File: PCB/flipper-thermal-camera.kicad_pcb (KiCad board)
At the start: 2 copper layers, 1 part, among them U1 MLX90640ESF-BAB-000-SP

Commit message: finish schematic
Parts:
- added C1: 100nF, Capacitor_SMD:C_0805_2012Metric, F.Cu at (81.9, 40.0)
- added C2: 100nF, Capacitor_SMD:C_0805_2012Metric, F.Cu at (81.9, 43.0)
- added C3: 100nF, Capacitor_SMD:C_0805_2012Metric, F.Cu at (81.9, 46.0)
- added C4: 100nF, Capacitor_SMD:C_0805_2012Metric, F.Cu at (81.9, 49.0)
- added C5: 1uF, Capacitor_SMD:C_0805_2012Metric, F.Cu at (81.9, 52.0)
- added C6: 4.7uF, Capacitor_SMD:C_0805_2012Metric, F.Cu at (81.9, 55.1)
- added D1: LED_R, LED_SMD:LED_0805_2012Metric, F.Cu at (86.4, 60.2)
- added D2: LED_G, LED_SMD:LED_0805_2012Metric, F.Cu at (86.4, 63.2)
- added IC1: VEML7700-TT, Components:XDCR_VEML7700-TT, F.Cu at (87.5, 54.5)
- added J1: Conn_01x08, Connector_PinHeader_2.54mm:PinHeader_1x08_P2.54mm_Horizontal, F.Cu at (148.5, 93.0)
- added J2: Conn_01x10, Connector_PinHeader_2.54mm:PinHeader_1x10_P2.54mm_Horizontal, F.Cu at (181.5, 93.0)
- added R1: 2.2k, Resistor_SMD:R_0805_2012Metric, F.Cu at (86.3, 40.0)
- added R2: 2.2k, Resistor_SMD:R_0805_2012Metric, F.Cu at (86.3, 42.9)
- added R3: 1.5k, Resistor_SMD:R_0805_2012Metric, F.Cu at (86.3, 45.9)
- added R4: 10k, Resistor_SMD:R_0805_2012Metric, F.Cu at (86.3, 48.8)
- added U2: XC6206PxxxMR, Package_TO_SOT_SMD:SOT-23-3, F.Cu at (91.1, 40.7)
- added U3: ICM-20948, Sensor_Motion:InvenSense_QFN-24_3x3mm_P0.4mm, F.Cu at (91.1, 45.5)
- added U4: SHT31-DIS, Sensor_Humidity:Sensirion_DFN-8-1EP_2.5x2.5mm_P0.5mm_EP1.1x1.7mm, F.Cu at (138.2, 70.5)
- moved U1 44.1 mm to (154.5, 68.9)
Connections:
- U1 pad 1: unconnected-(U1-SDA-Pad1) -> /SDA
- U1 pad 2: unconnected-(U1-VDD-Pad2) -> +3V3
- U1 pad 3: unconnected-(U1-GND-Pad3) -> GND
- U1 pad 4: unconnected-(U1-SCL-Pad4) -> /SCL
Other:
- board text added: "1"
- board text added: "10"
- board text added: "11"
- board text added: "12"
- board text added: "13"
- board text added: "14"
- board text added: "15"
- board text added: "16"
- board text added: "17"
- board text added: "18"
- board text added: "2"
- board text added: "3"
- board text added: "4"
- board text added: "5"
- board text added: "6"
- board text added: "7"
- board text added: "8"
- board text added: "9"

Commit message: finish routing pcb
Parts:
- removed J1: Conn_01x08, Connector_PinHeader_2.54mm:PinHeader_1x08_P2.54mm_Horizontal
- removed J2: Conn_01x10, Connector_PinHeader_2.54mm:PinHeader_1x10_P2.54mm_Horizontal
- added A1: Flipper_Zero, Module:Flipper_Zero_Angled, F.Cu at (123.5, 88.2)
- IC1, U1: moved to B.Cu
- moved C1 105.3 mm to (181.8, 73.4)
- moved R2 100.1 mm to (178.4, 82.2), turned to 90 degrees
- moved R1 99.5 mm to (176.4, 82.2), turned to 90 degrees
- moved C3 97.5 mm to (176.5, 69.8), turned to 90 degrees
- moved C2 95.8 mm to (171.8, 76.2), turned to 90 degrees
- moved U3 90.9 mm to (176.7, 76.2), turned to 180 degrees
- moved R4 82.8 mm to (164.6, 76.0), turned to 90 degrees
- moved C4 78.4 mm to (151.8, 84.6), turned to 180 degrees
- moved IC1 67.3 mm to (153.2, 69.4), turned to 90 degrees
- moved C5 57.3 mm to (130.6, 82.3), turned to -90 degrees
- moved U2 54.7 mm to (126.9, 82.1), turned to -90 degrees
- moved C6 50.6 mm to (127.1, 77.9), turned to 180 degrees
- moved R3 48.1 mm to (120.8, 79.5), turned to -90 degrees
- moved D2 40.1 mm to (126.0, 69.5)
- moved D1 37.1 mm to (122.2, 69.5)
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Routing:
- net +3V3: track 0.00 -> 154.9 mm, vias 0 -> 2
- net /SDA: track 0.00 -> 62.9 mm, vias 0 -> 1
- net /SCL: track 0.00 -> 53.9 mm, vias 0 -> 3
- net +5V: track 0.00 -> 19.0 mm
- net GND: track 0.00 -> 16.5 mm, vias 0 -> 44
- net /INT_1: track 0.00 -> 16.4 mm, vias 0 -> 1
- net /TMP_RST: track 0.00 -> 14.1 mm, vias 0 -> 1
- net Net-(D1-A): track 0.00 -> 10.1 mm
- net Net-(U3-REGOUT): track 0.00 -> 4.07 mm
- added copper zone on B.Cu, net GND
- added copper zone on F.Cu, net GND
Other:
- board outline added: 67.4 x 20 mm
- board text added: "3V3"
- board text added: "5V"
- board text added: "Flipper Thermal Camera By Evan Yu"
- board text added: "v1.0"

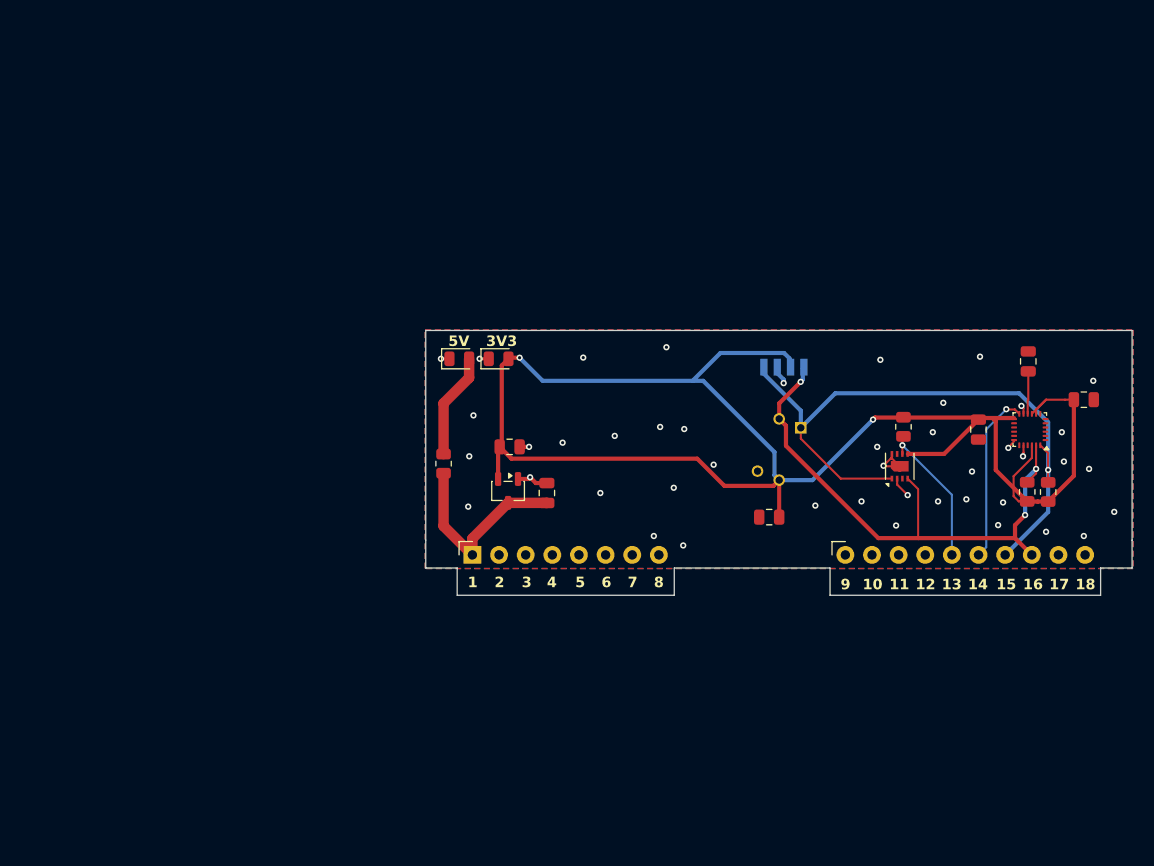
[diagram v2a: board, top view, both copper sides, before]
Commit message: add testpoints
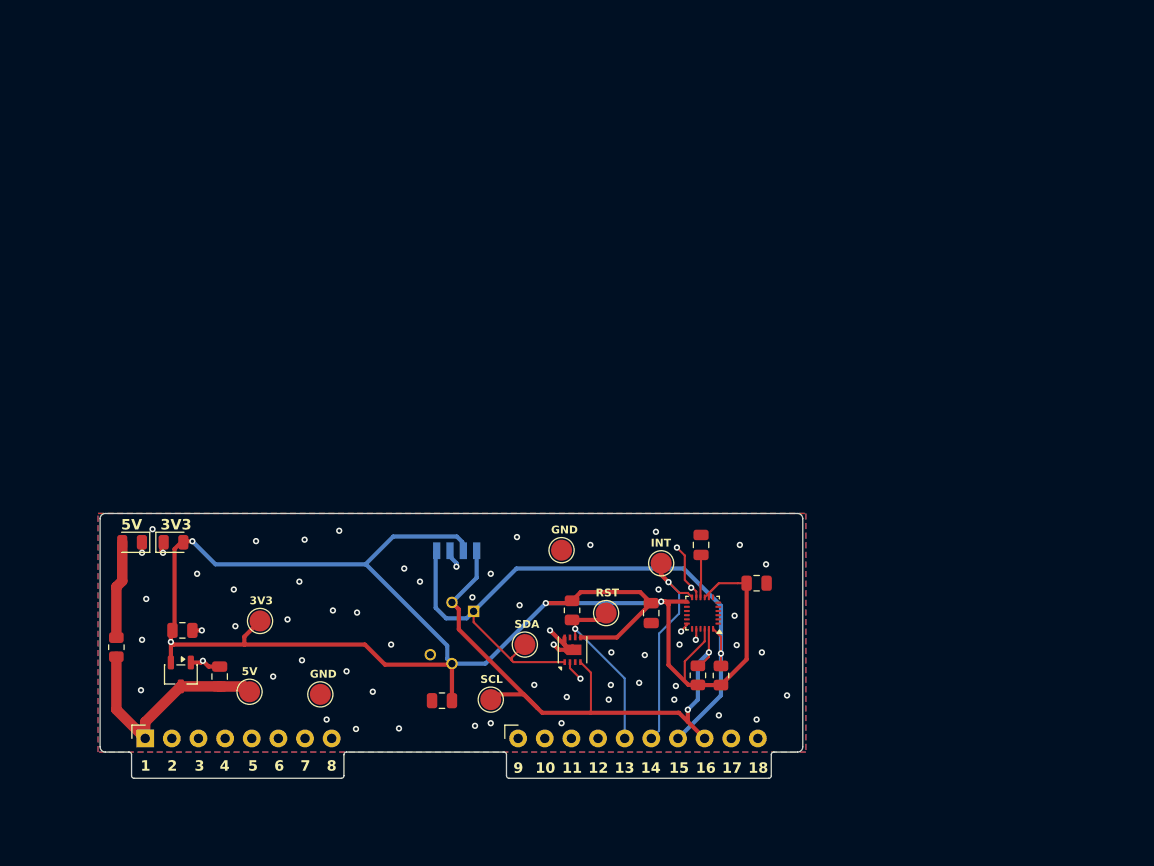
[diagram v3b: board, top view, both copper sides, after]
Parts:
- added SDA1: GND, TestPoint:TestPoint_Pad_D2.0mm, F.Cu at (128.5, 96.8)
- added TP1: 3V3, TestPoint:TestPoint_Pad_D2.0mm, F.Cu at (103.2, 94.5)
- added TP2: 5V, TestPoint:TestPoint_Pad_D2.0mm, F.Cu at (102.2, 101.2)
- added TP3: GND, TestPoint:TestPoint_Pad_D2.0mm, F.Cu at (109.0, 101.5)
- added TP4: GND, TestPoint:TestPoint_Pad_D2.0mm, F.Cu at (132.0, 87.8)
- added TP5: SCL, TestPoint:TestPoint_Pad_D2.0mm, F.Cu at (125.2, 102.0)
- added TP6: TMP_SENS_RST, TestPoint:TestPoint_Pad_D2.0mm, F.Cu at (136.2, 93.8)
- added TP7: INT_ICM, TestPoint:TestPoint_Pad_D2.0mm, F.Cu at (141.5, 89.0)
- moved R4 36.1 mm to (133.0, 93.5)
- moved R1 35.9 mm to (145.0, 99.7)
- moved C1 35.8 mm to (150.6, 90.9)
- moved C4 35.8 mm to (120.6, 102.1)
- moved R2 35.8 mm to (147.2, 99.7)
- moved U3 35.8 mm to (145.4, 93.8)
- moved A1 35.8 mm to (92.3, 105.7)
- moved D1 35.8 mm to (91.0, 87.0), turned to 180 degrees
- moved R3 35.8 mm to (89.5, 97.0)
- moved U1 35.8 mm to (121.5, 95.7)
- moved U2 35.8 mm to (95.7, 99.6)
- moved C2 35.8 mm to (140.6, 93.8)
- moved C3 35.8 mm to (145.3, 87.2)
- moved C5 35.8 mm to (99.4, 99.8)
- moved C6 35.8 mm to (95.9, 95.4)
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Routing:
- net +3V3: track 154.9 -> 168.1 mm, vias 2 -> 4
- net GND: track 16.5 -> 23.0 mm, vias 44 -> 64
- net /SDA: track 62.9 -> 67.9 mm
- net /INT_1: track 16.4 -> 21.4 mm
- net /SCL: track 53.9 -> 57.8 mm, vias 3 -> 2
- net /TMP_RST: track 14.1 -> 17.5 mm
- net +5V: track 19.0 -> 22.1 mm
- net Net-(D1-A): track 10.1 -> 9.32 mm
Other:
- board size 67.4 x 20 mm -> 67 x 25.2 mm
- board text added: "GND"
- board text added: "INT"
- board text added: "RST"
- board text added: "SCL"
- board text added: "SDA"

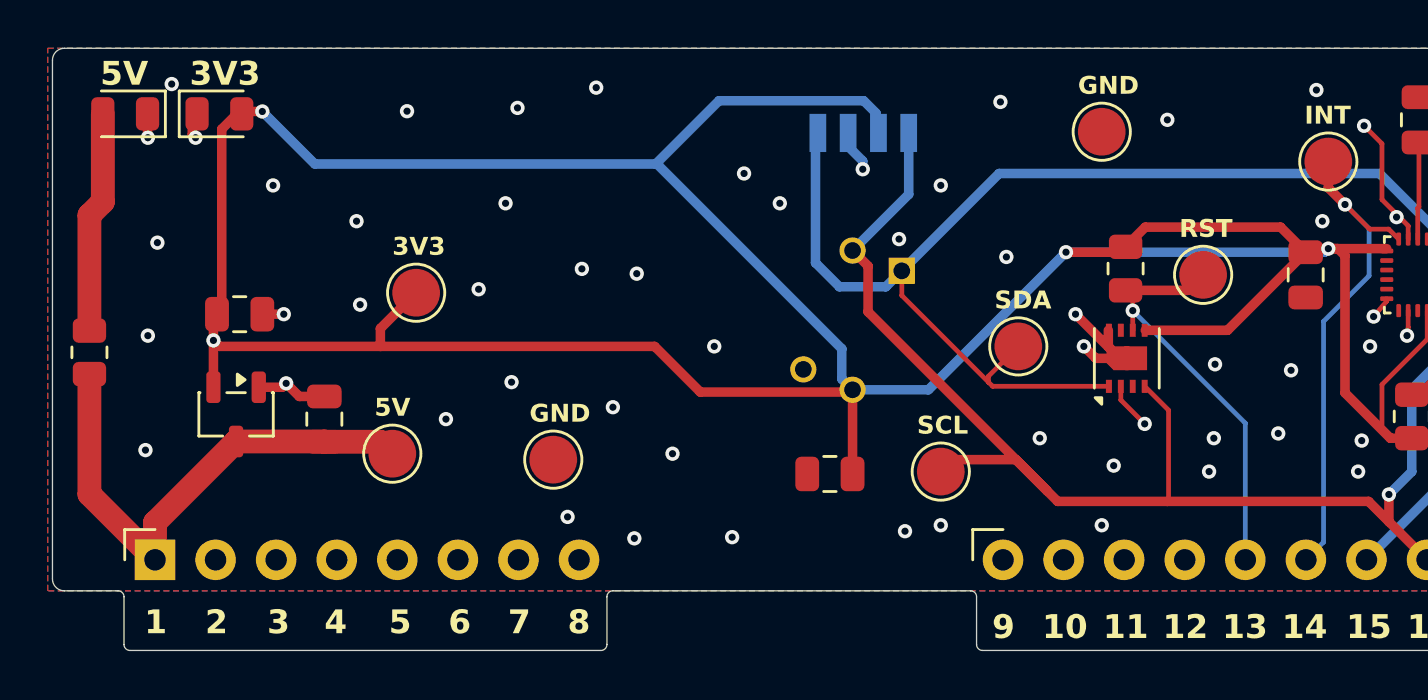
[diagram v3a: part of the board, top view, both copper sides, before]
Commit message: source parts
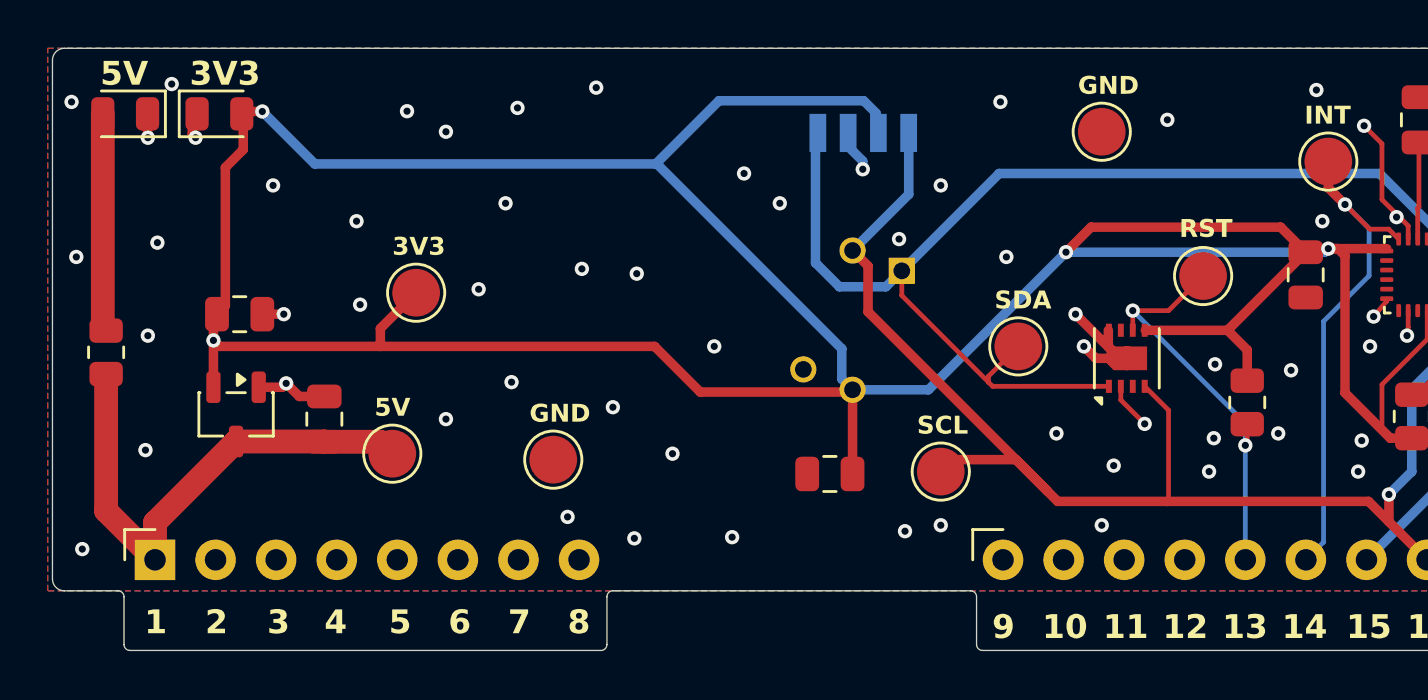
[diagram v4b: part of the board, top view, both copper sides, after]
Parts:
- moved R4 7.58 mm to (138.1, 99.1)
- moved R3 0.70 mm to (90.2, 97.0)
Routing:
- net +3V3: track 168.1 -> 170.8 mm
- net /TMP_RST: track 17.5 -> 17.7 mm, vias 1 -> 2
- net GND: vias 64 -> 68

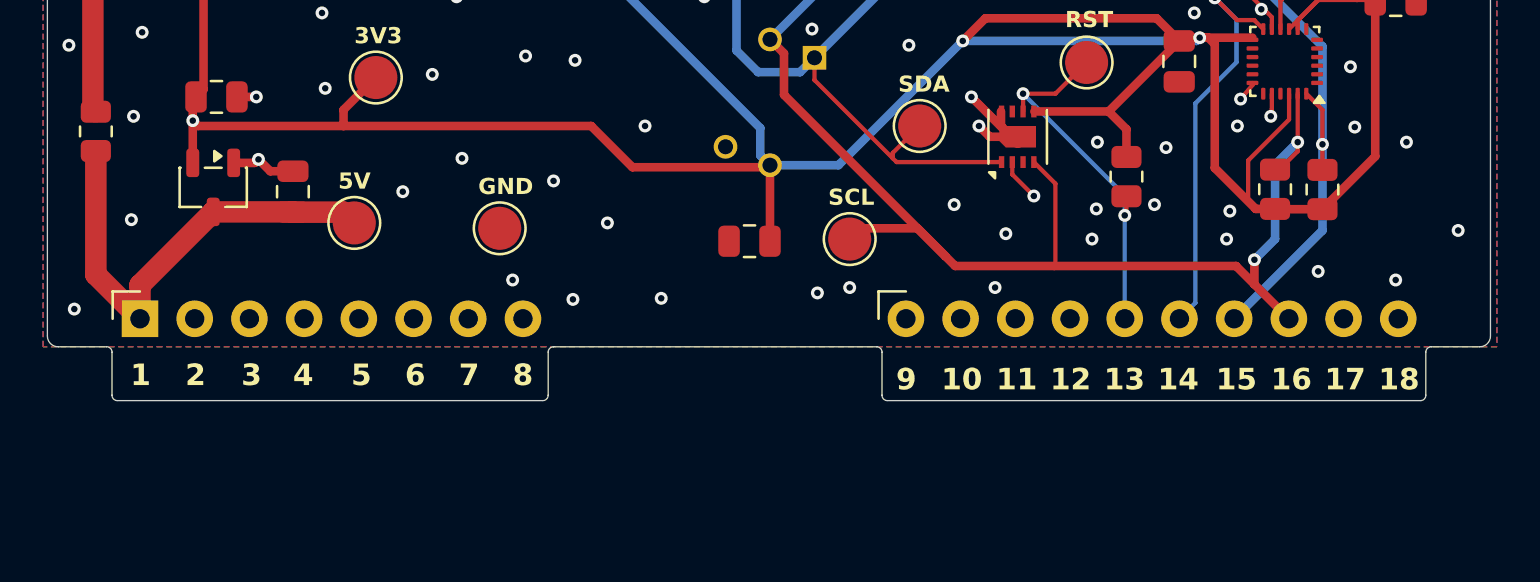
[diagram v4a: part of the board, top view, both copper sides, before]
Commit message: add bom
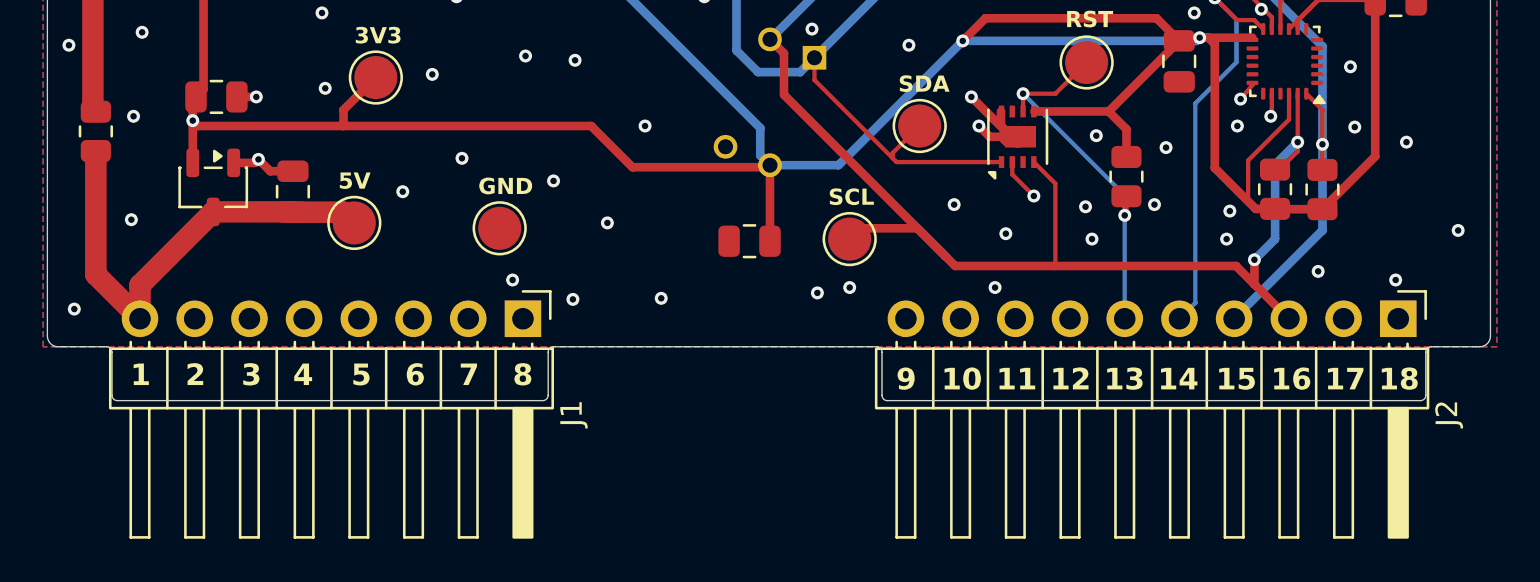
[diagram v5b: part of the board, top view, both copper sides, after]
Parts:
- removed A1: Flipper_Zero, Module:Flipper_Zero_Angled
- added J1: Conn_01x08, Connector_PinHeader_2.54mm:PinHeader_1x08_P2.54mm_Horizontal, F.Cu at (110.1, 105.7)
- added J2: Conn_01x10, Connector_PinHeader_2.54mm:PinHeader_1x10_P2.54mm_Horizontal, F.Cu at (150.7, 105.7)
